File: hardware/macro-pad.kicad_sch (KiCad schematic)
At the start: 41 parts, among them J1 USB_C_Receptacle_USB2.0, SW1 PEC12R-4025F-S0024, SW2 MX1A-G1NA, SW3 MX1A-G1NA, SW4 MX1A-G1NA, SW5 MX1A-G1NA, U1 MIC5317-3.3ZD5-TR, U2 RP2040, U3 W25Q128JVSIQ, Y1 ABLS-12.000MHZ-B4-T

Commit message: Replaced capacitor footprints with bigger ones
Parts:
- C1, C10, C11, C12, C13, C14, C15, C16, C17, C18, C19, C2, C20, C3, C4, C5, C6, C7, C8, C9: footprint Capacitor_SMD:C_0201_0603Metric_Pad0.64x0.40mm_HandSolder -> Capacitor_SMD:C_0603_1608Metric_Pad1.08x0.95mm_HandSolder

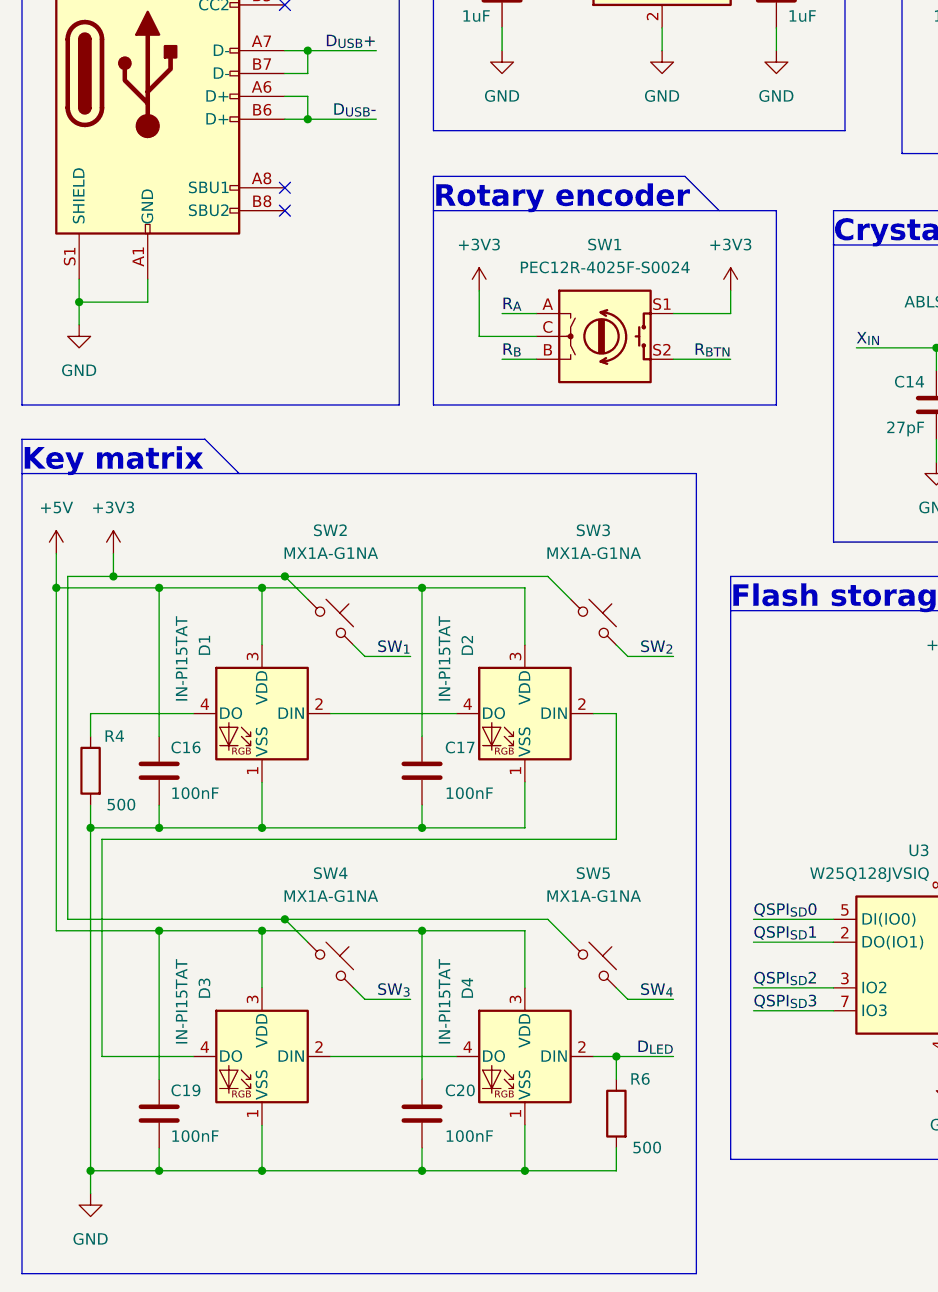
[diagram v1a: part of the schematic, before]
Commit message: Wired swicthes to be pulled down if actived instead of up
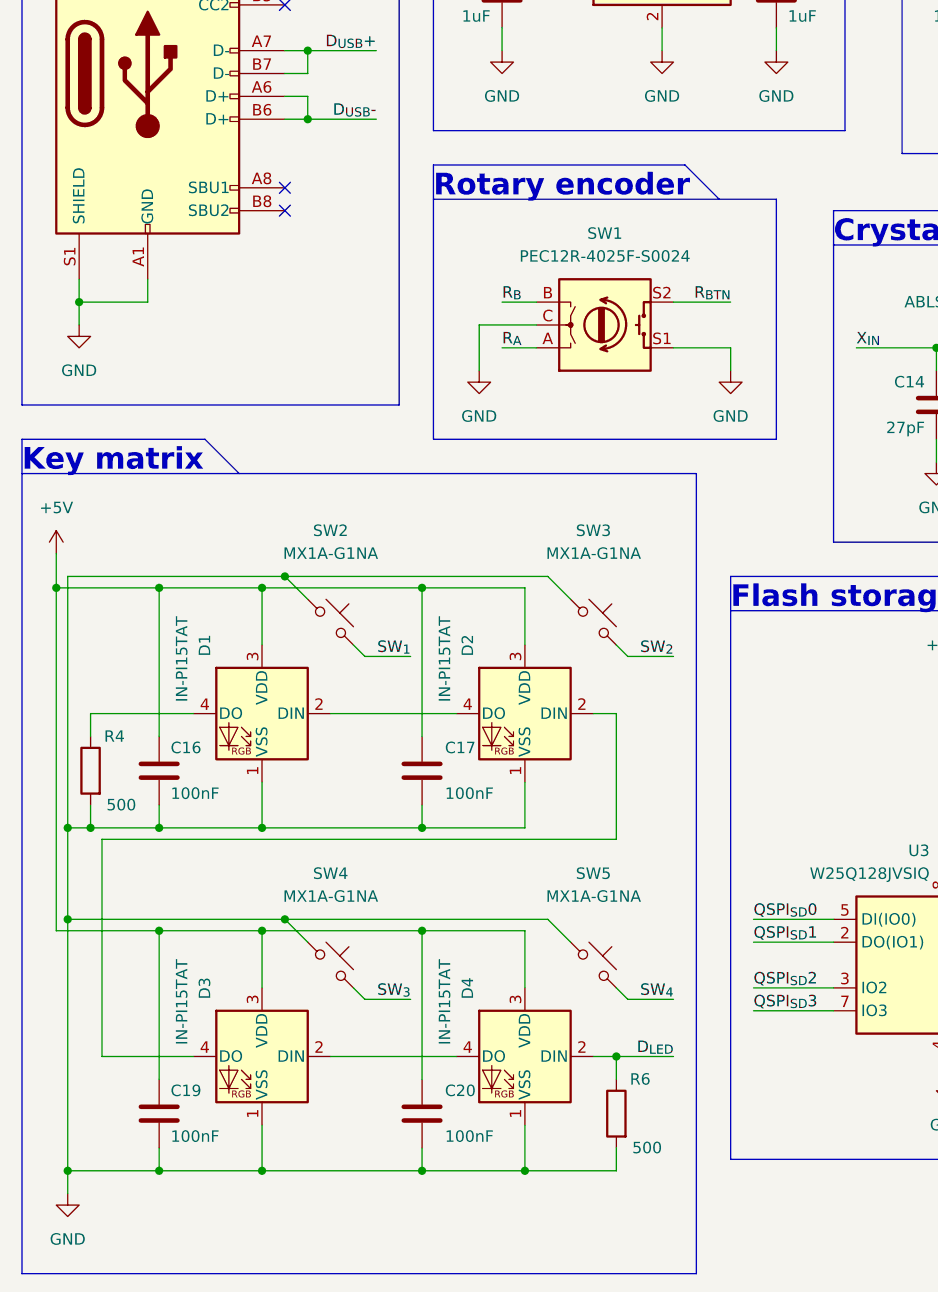
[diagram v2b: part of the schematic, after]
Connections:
- net +3V3: no longer SW1.C, SW1.S1, SW2.1, SW3.1, SW4.1, SW5.1
- net GND: now also SW1.C, SW1.S1, SW2.1, SW3.1, SW4.1, SW5.1
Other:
- moved on the sheet: SW1

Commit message: Corrected SMD LED footprint
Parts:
- D1, D2, D3, D4: footprint LED_SMD:LED_Inolux_IN-PI554FCH_PLCC4_5.0x5.0mm_P3.2mm -> LED_SMD:LED_SK6812_EC15_1.5x1.5mm
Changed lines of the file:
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@@
       (effects (font (size 1.27 1.27)) (justify left))
     )
-    (property "Footprint" "LED_SMD:LED_Inolux_IN-PI554FCH_PLCC4_5.0x5.0mm_P3.2mm" (id 2) (at 80.01 130.81 0)
+    (property "Footprint" "LED_SMD:LED_SK6812_EC15_1.5x1.5mm" (id 2) (at 80.01 130.81 0)
       (effects (font (size 1.27 1.27)) (justify left top) hide)
     )
@@
   (symbol (lib_id "power:GND") (at 76.2 85.09 0) (unit 1)
     (in_bom yes) (on_board yes) (fields_autoplaced)
-    (property "Reference" "#PWR?" (id 0) (at 76.2 91.44 0)
+    (property "Reference" "#PWR0102" (id 0) (at 76.2 91.44 0)
       (effects (font (size 1.27 1.27)) hide)
     )
@@
   (symbol (lib_id "power:GND") (at 104.14 85.09 0) (unit 1)
     (in_bom yes) (on_board yes) (fields_autoplaced)
-    (property "Reference" "#PWR?" (id 0) (at 104.14 91.44 0)
+    (property "Reference" "#PWR0101" (id 0) (at 104.14 91.44 0)
       (effects (font (size 1.27 1.27)) hide)
     )
@@
       (effects (font (size 1.27 1.27)) (justify left))
     )
-    (property "Footprint" "LED_SMD:LED_Inolux_IN-PI554FCH_PLCC4_5.0x5.0mm_P3.2mm" (id 2) (at 50.8 130.81 0)
+    (property "Footprint" "LED_SMD:LED_SK6812_EC15_1.5x1.5mm" (id 2) (at 50.8 130.81 0)
       (effects (font (size 1.27 1.27)) (justify left top) hide)
     )
@@
       (effects (font (size 1.27 1.27)) (justify left))
     )
-    (property "Footprint" "LED_SMD:LED_Inolux_IN-PI554FCH_PLCC4_5.0x5.0mm_P3.2mm" (id 2) (at 80.01 168.91 0)
+    (property "Footprint" "LED_SMD:LED_SK6812_EC15_1.5x1.5mm" (id 2) (at 80.01 168.91 0)
       (effects (font (size 1.27 1.27)) (justify left top) hide)
     )
@@
       (effects (font (size 1.27 1.27)) (justify left))
     )
-    (property "Footprint" "LED_SMD:LED_Inolux_IN-PI554FCH_PLCC4_5.0x5.0mm_P3.2mm" (id 2) (at 50.8 168.91 0)
+    (property "Footprint" "LED_SMD:LED_SK6812_EC15_1.5x1.5mm" (id 2) (at 50.8 168.91 0)
       (effects (font (size 1.27 1.27)) (justify left top) hide)
     )
@@
       (reference "#PWR025") (unit 1) (value "GND") (footprint "")
     )
+    (path "/71ca22fd-6f1e-4536-87f9-d0864b125d1d"
+      (reference "#PWR0101") (unit 1) (value "GND") (footprint "")
+    )
     (path "/62c929bd-6f26-4578-bfff-98f3c42f1083"
-      (reference "#PWR?") (unit 1) (value "GND") (footprint "")
-    )
-    (path "/71ca22fd-6f1e-4536-87f9-d0864b125d1d"
-      (reference "#PWR?") (unit 1) (value "GND") (footprint "")
+      (reference "#PWR0102") (unit 1) (value "GND") (footprint "")
     )
     (path "/d3290334-df8d-42fb-8f84-c8b579cd4c2d"
@@
     )
     (path "/730a4d99-f88d-41ed-9938-4e5443708e7b"
-      (reference "D1") (unit 1) (value "IN-PI15TAT") (footprint "LED_SMD:LED_Inolux_IN-PI554FCH_PLCC4_5.0x5.0mm_P3.2mm")
+      (reference "D1") (unit 1) (value "IN-PI15TAT") (footprint "LED_SMD:LED_SK6812_EC15_1.5x1.5mm")
     )
     (path "/02452c7e-d830-484b-b64b-2b3b9ee41336"
-      (reference "D2") (unit 1) (value "IN-PI15TAT") (footprint "LED_SMD:LED_Inolux_IN-PI554FCH_PLCC4_5.0x5.0mm_P3.2mm")
+      (reference "D2") (unit 1) (value "IN-PI15TAT") (footprint "LED_SMD:LED_SK6812_EC15_1.5x1.5mm")
     )
     (path "/c8178cb7-f2f1-4a6e-86dd-9889553ad2db"
-      (reference "D3") (unit 1) (value "IN-PI15TAT") (footprint "LED_SMD:LED_Inolux_IN-PI554FCH_PLCC4_5.0x5.0mm_P3.2mm")
+      (reference "D3") (unit 1) (value "IN-PI15TAT") (footprint "LED_SMD:LED_SK6812_EC15_1.5x1.5mm")
     )
     (path "/b720d4e0-282d-4058-ba67-1f35dd1733ac"
-      (reference "D4") (unit 1) (value "IN-PI15TAT") (footprint "LED_SMD:LED_Inolux_IN-PI554FCH_PLCC4_5.0x5.0mm_P3.2mm")
+      (reference "D4") (unit 1) (value "IN-PI15TAT") (footprint "LED_SMD:LED_SK6812_EC15_1.5x1.5mm")
     )
     (path "/e325433c-a087-465d-b143-a8822076c064"

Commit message: Set resistors and capacitors to use a smaller footprint and chnaged to non-handsolder
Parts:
- C1, C10, C11, C12, C13, C14, C15, C16, C17, C18, C19, C2, C20, C3, C4, C5, C6, C7, C8, C9: footprint Capacitor_SMD:C_0603_1608Metric_Pad1.08x0.95mm_HandSolder -> Capacitor_SMD:C_0402_1005Metric
- R1, R2, R3, R4, R5, R6: footprint Resistor_SMD:R_0603_1608Metric_Pad0.98x0.95mm_HandSolder -> Resistor_SMD:R_0402_1005Metric
- Y1: footprint Crystal:Crystal_SMD_HC49-SD_HandSoldering -> Crystal:Crystal_SMD_HC49-SD

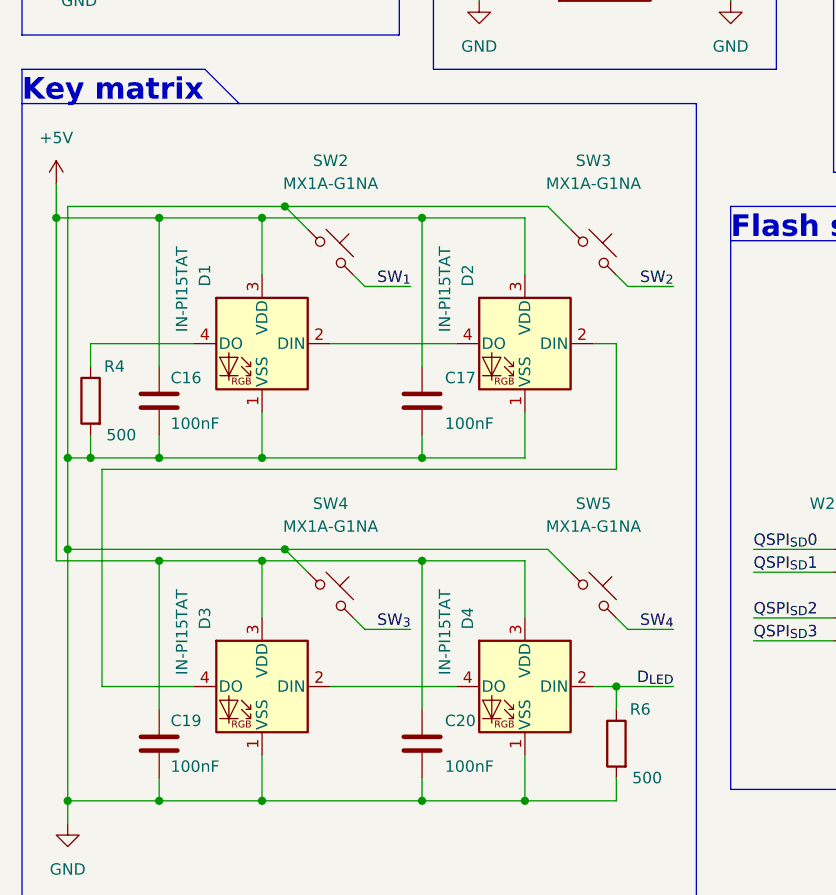
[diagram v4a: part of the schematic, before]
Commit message: Reversed RGB LED data path for easier routing
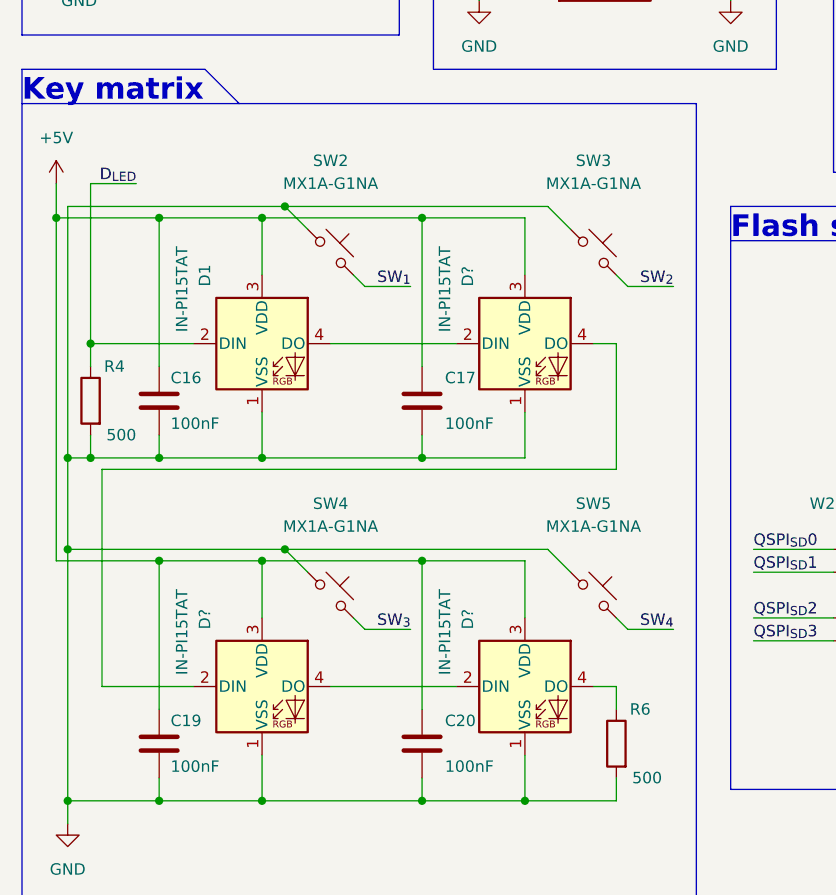
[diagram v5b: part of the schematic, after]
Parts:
- removed D2, D3, D4: IN-PI15TAT, LED_SMD:LED_SK6812_EC15_1.5x1.5mm, symbol LED:Inolux_IN-PI554FCH
- added D? (x3): IN-PI15TAT, LED_SMD:LED_SK6812_EC15_1.5x1.5mm, symbol LED:Inolux_IN-PI554FCH
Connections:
- net +5V: now also D?.3 (VDD), D?.3 (VDD), D?.3 (VDD)
- net D_{LED}: now also D1.2 (DIN), R4.1; no longer R6.1
- net GND: now also D?.1 (VSS), D?.1 (VSS), D?.1 (VSS)
- net at D1.4 (DO): now also D?.2 (DIN); no longer R4.1
- new net: D?.2 (DIN), D?.4 (DO) (x2)
- new net: D?.4 (DO), R6.1
